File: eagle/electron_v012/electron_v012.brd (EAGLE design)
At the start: 20.3 x 50.8 mm, 92 parts, among them J1 SIM-NANO-4FF, J2 IPEX-20279-001E, U1 U-BLOX-SARA-U260, U2 SN74AVC4T245, U3 STM32F205RG, U4 MAX1704X, U5 SN74LVC1G07, U6 SN74LVC1G07, U8 SN74AVC4T245, X1 USB-MICROB, Y1 32Khz, Y2 26Mhz

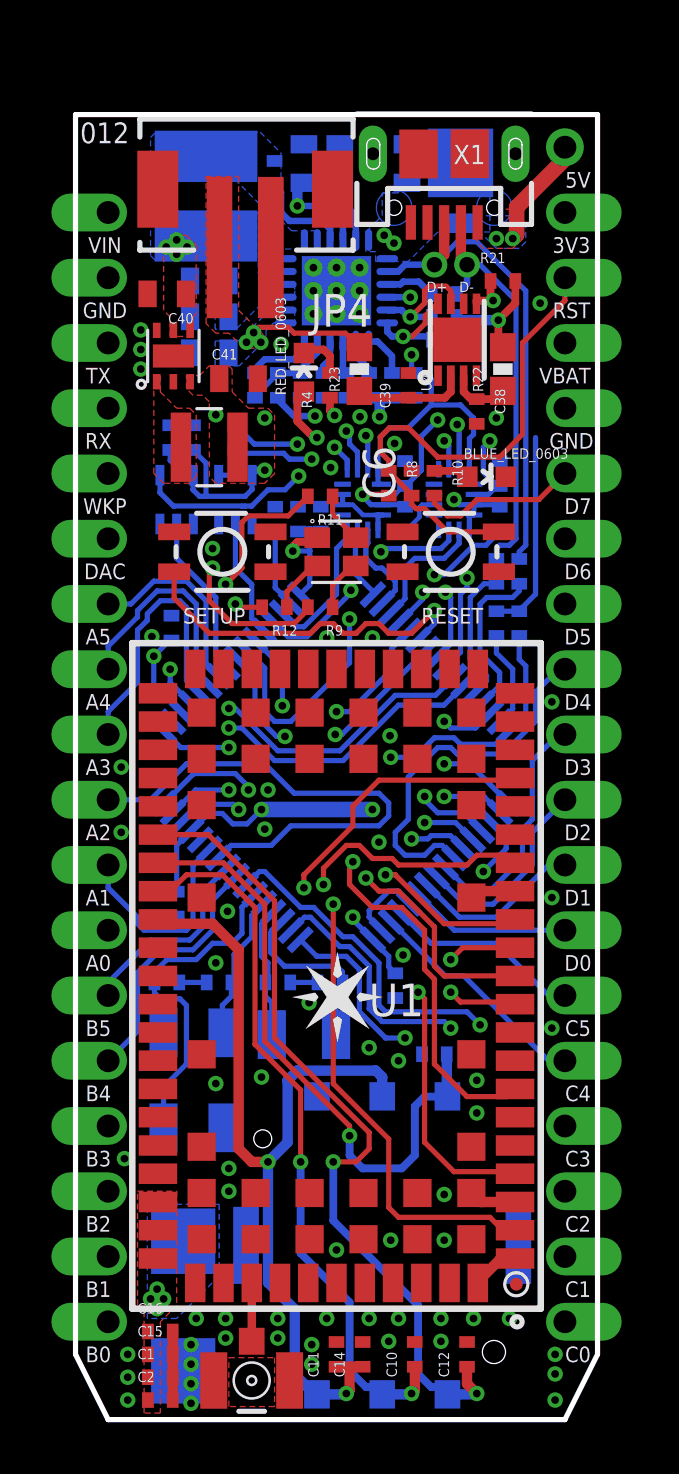
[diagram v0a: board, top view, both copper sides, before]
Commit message: added lipo and pmid 5v header
change log:
1. Exposed LiPo connection via a header
2. Exposed PMID boost 5V via a header
3. Lowered the 3V3 inductor and rotated its output cap to meet
datasheet recommendations
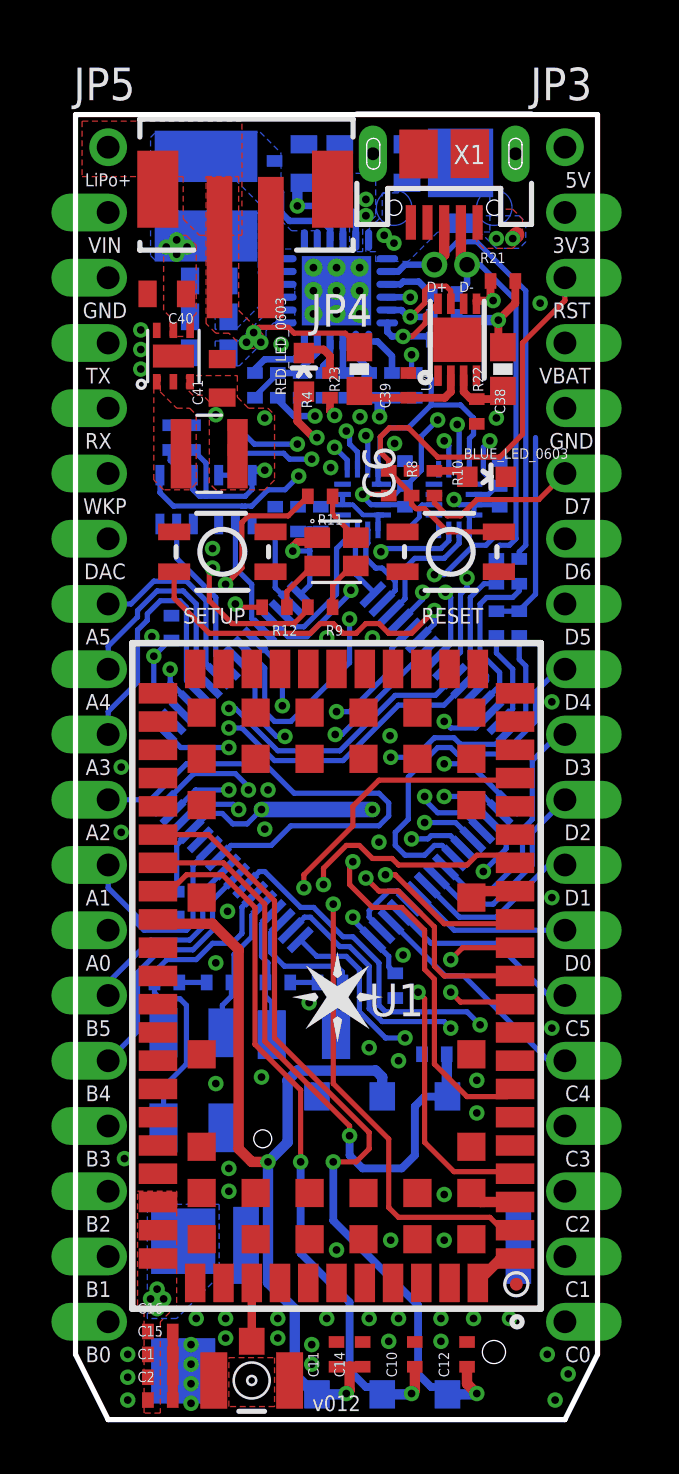
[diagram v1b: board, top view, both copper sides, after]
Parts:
- added JP5: (no value), Particle:1X01_NO_SILK
- JP3: device Particle:1X01 -> Particle:1X01_NO_SILK
- moved C41 0.63 mm to (5.71, 40.5), turned to 90 degrees
- moved U$6 0.25 mm to (5.20, 37.6)
- flipped JP3 to the top
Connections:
- net BAT: now also JP5.1
- net PMID: now also JP3.1
- net VBUS: no longer JP3.1
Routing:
- net PMID: track 2.49 -> 11.9 mm, vias 0 -> 2
- net VBUS: track 4.40 -> 0.22 mm
- added copper zone on layer 16, net PMID
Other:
- board text added: "LiPo+"
- board text added: "v012"
- board text removed: "012"
